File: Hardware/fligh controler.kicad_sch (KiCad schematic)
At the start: 0 parts

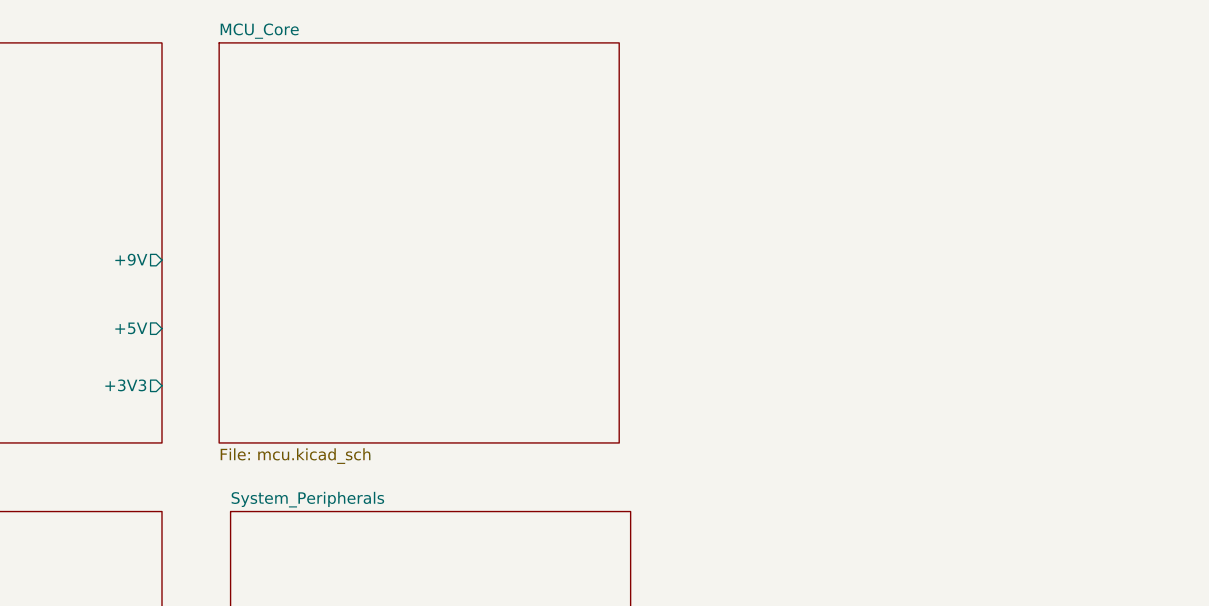
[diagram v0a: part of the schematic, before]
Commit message: feat(mcu): finalize core schematic and update project documentation
- MCU_Core: Completed pin definitions and Hierarchical Labels (SPI, UART, I2C, Motors).
- Root: Updated sheet pins to reflect the new MCU architecture.
- Docs: Refined README.md with detailed hierarchical roadmap and MIT License.
- Docs: Added 'Connectors & I/O' breakdown to the development plan.
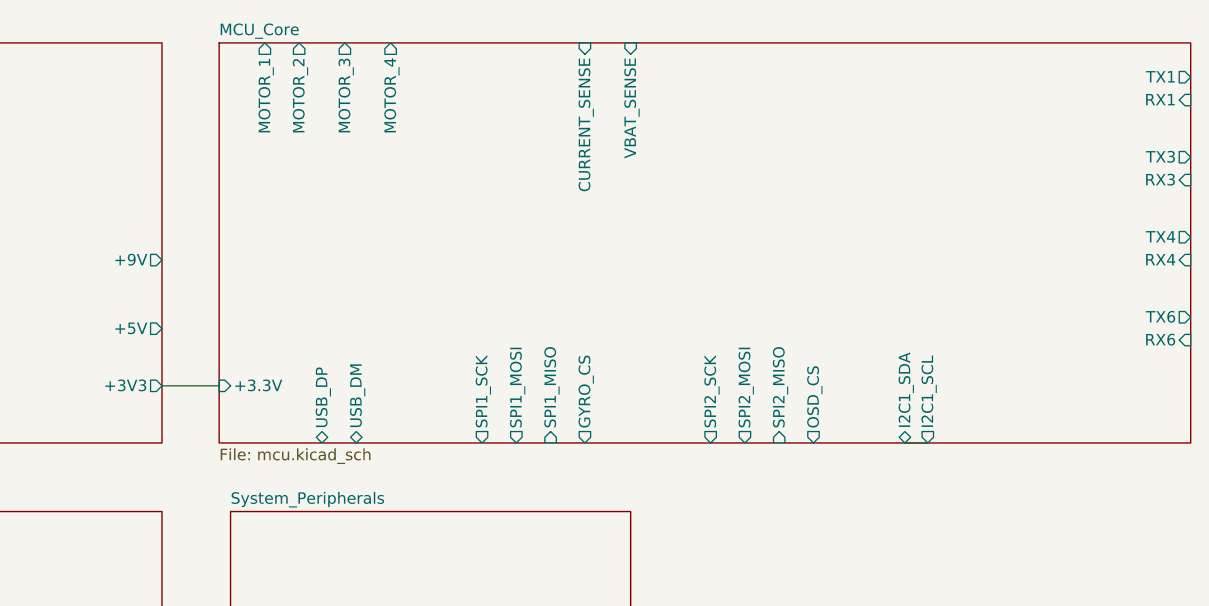
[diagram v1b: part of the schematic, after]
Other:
- sheet MCU_Core ports: added +3.3V, CURRENT_SENSE, GYRO_CS, I2C1_SCL, I2C1_SDA, MOTOR_1, MOTOR_2, MOTOR_3, MOTOR_4, OSD_CS, RX1, RX3, RX4, RX6, SPI1_MISO, SPI1_MOSI, SPI1_SCK, SPI2_MISO, SPI2_MOSI, SPI2_SCK, TX1, TX3, TX4, TX6, USB_DM, USB_DP, VBAT_SENSE; removed none

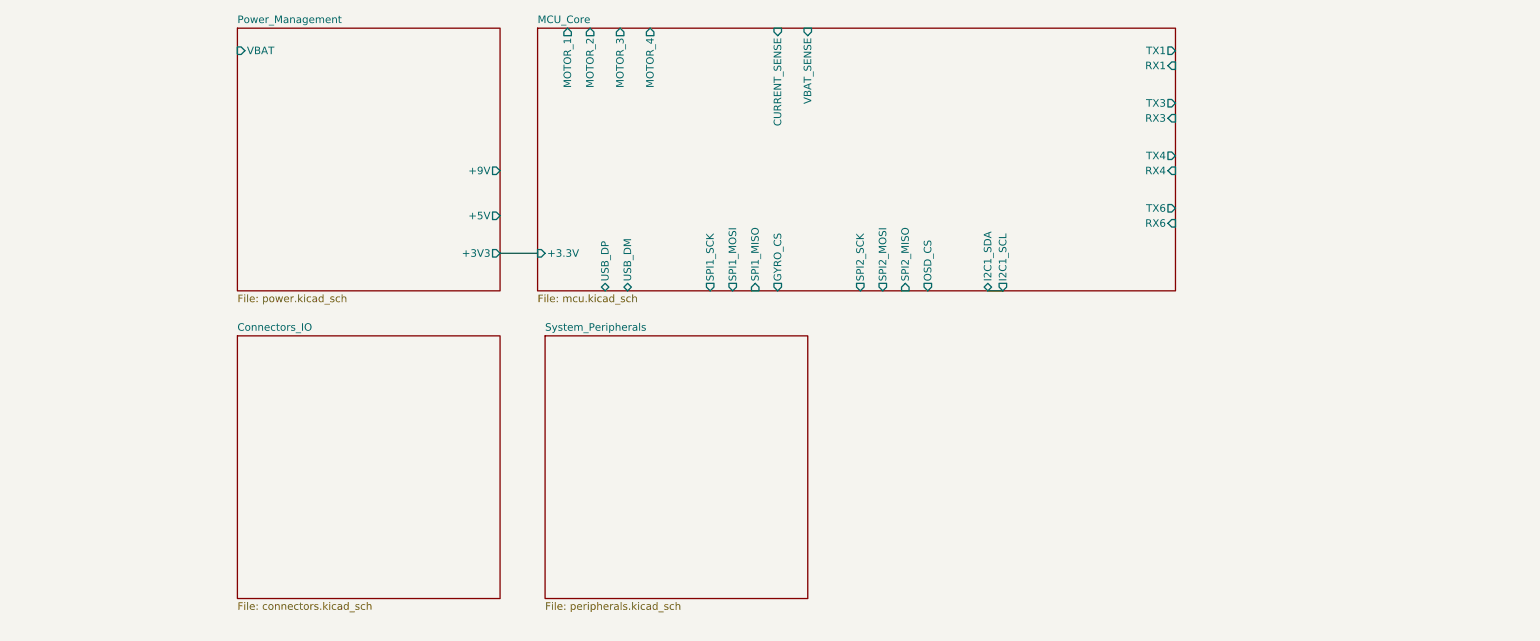
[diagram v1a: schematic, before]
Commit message: feat: implement system peripherals (OSD, Gyro, Baro)
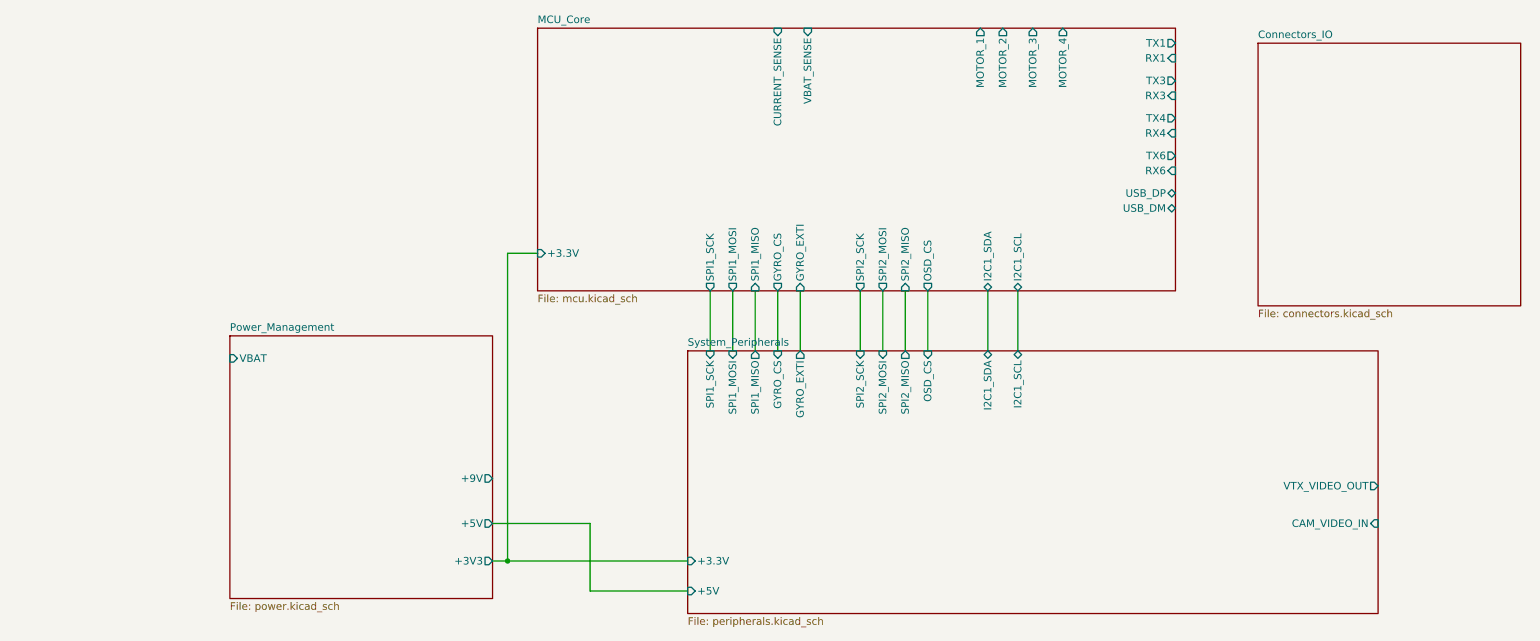
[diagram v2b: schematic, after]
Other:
- sheet MCU_Core ports: added GYRO_EXTI; removed none
- sheet System_Peripherals ports: added +3.3V, +5V, CAM_VIDEO_IN, GYRO_CS, GYRO_EXTI, I2C1_SCL, I2C1_SDA, OSD_CS, SPI1_MISO, SPI1_MOSI, SPI1_SCK, SPI2_MISO, SPI2_MOSI, SPI2_SCK, VTX_VIDEO_OUT; removed none

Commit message: Finalize schematic: Add connectors, LEDs, Buzzer and fix all ERC errors
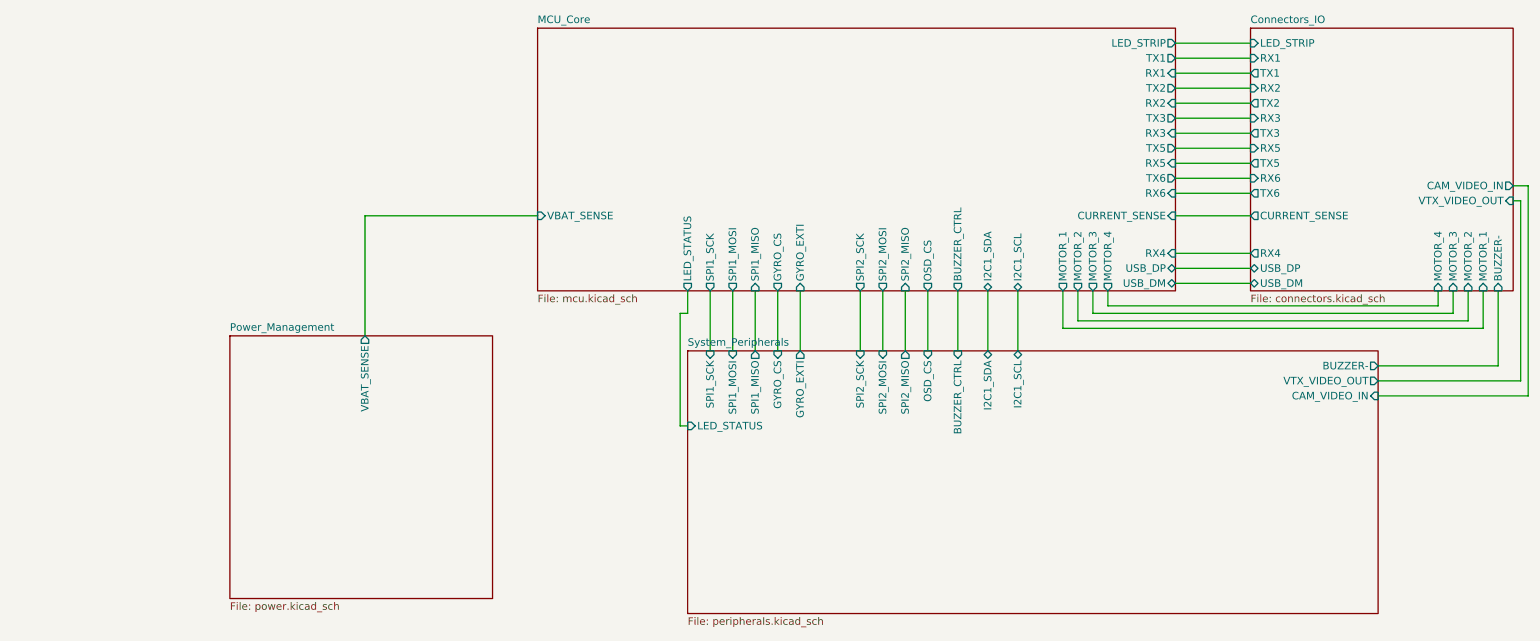
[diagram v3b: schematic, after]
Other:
- sheet Connectors_IO ports: added BUZZER-, CAM_VIDEO_IN, CURRENT_SENSE, LED_STRIP, MOTOR_1, MOTOR_2, MOTOR_3, MOTOR_4, RX1, RX2, RX3, RX4, RX5, RX6, TX1, TX2, TX3, TX5, TX6, USB_DM, USB_DP, VTX_VIDEO_OUT; removed none
- sheet MCU_Core ports: added BUZZER_CTRL, LED_STATUS, LED_STRIP, RX2, RX5, TX2, TX5; removed +3.3V, TX4
- sheet Power_Management ports: added VBAT_SENSE; removed +3V3, +5V, +9V, VBAT
- sheet System_Peripherals ports: added BUZZER-, BUZZER_CTRL, LED_STATUS; removed +3.3V, +5V

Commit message: Update schematic: Add SDIO Blackbox, ESC Redundancy and remove UART5
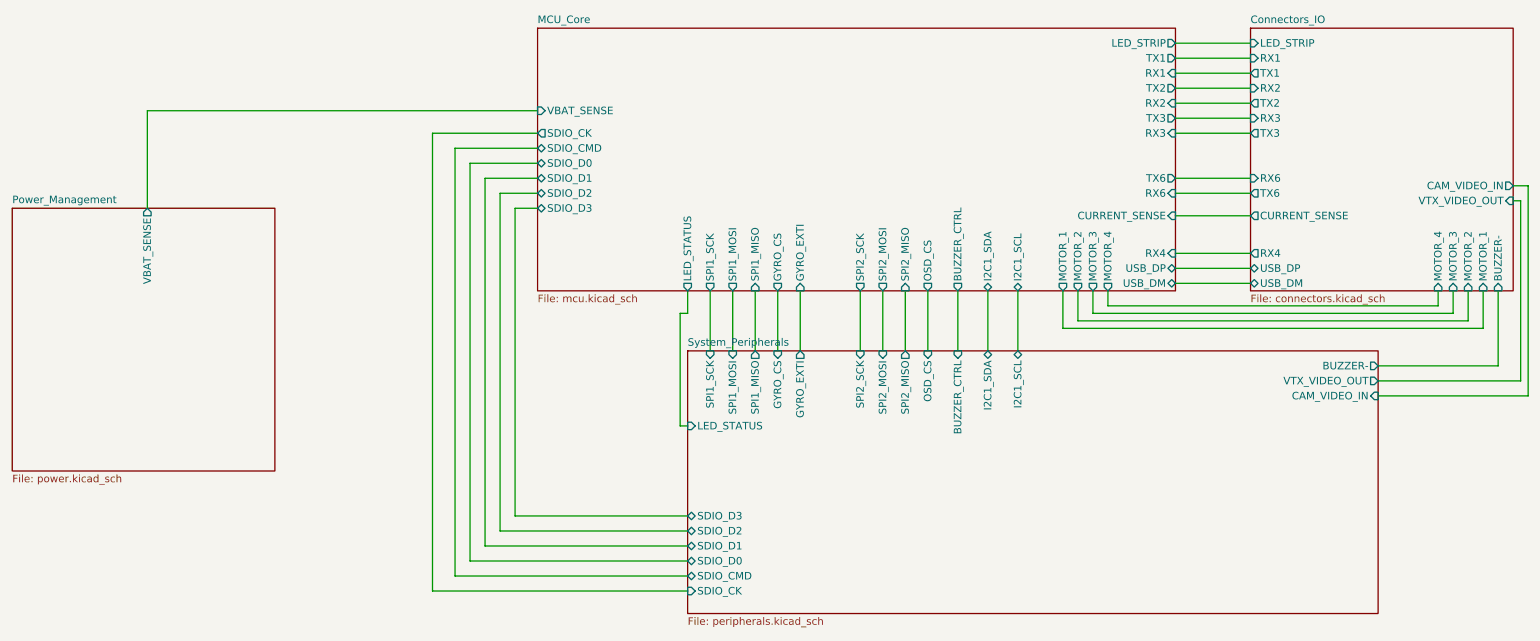
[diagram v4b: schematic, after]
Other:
- sheet Connectors_IO ports: added none; removed RX5, TX5
- sheet MCU_Core ports: added SDIO_CK, SDIO_CMD, SDIO_D0, SDIO_D1, SDIO_D2, SDIO_D3; removed RX5, TX5
- sheet System_Peripherals ports: added SDIO_CK, SDIO_CMD, SDIO_D0, SDIO_D1, SDIO_D2, SDIO_D3; removed none
